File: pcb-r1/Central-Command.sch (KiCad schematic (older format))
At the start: 3 parts

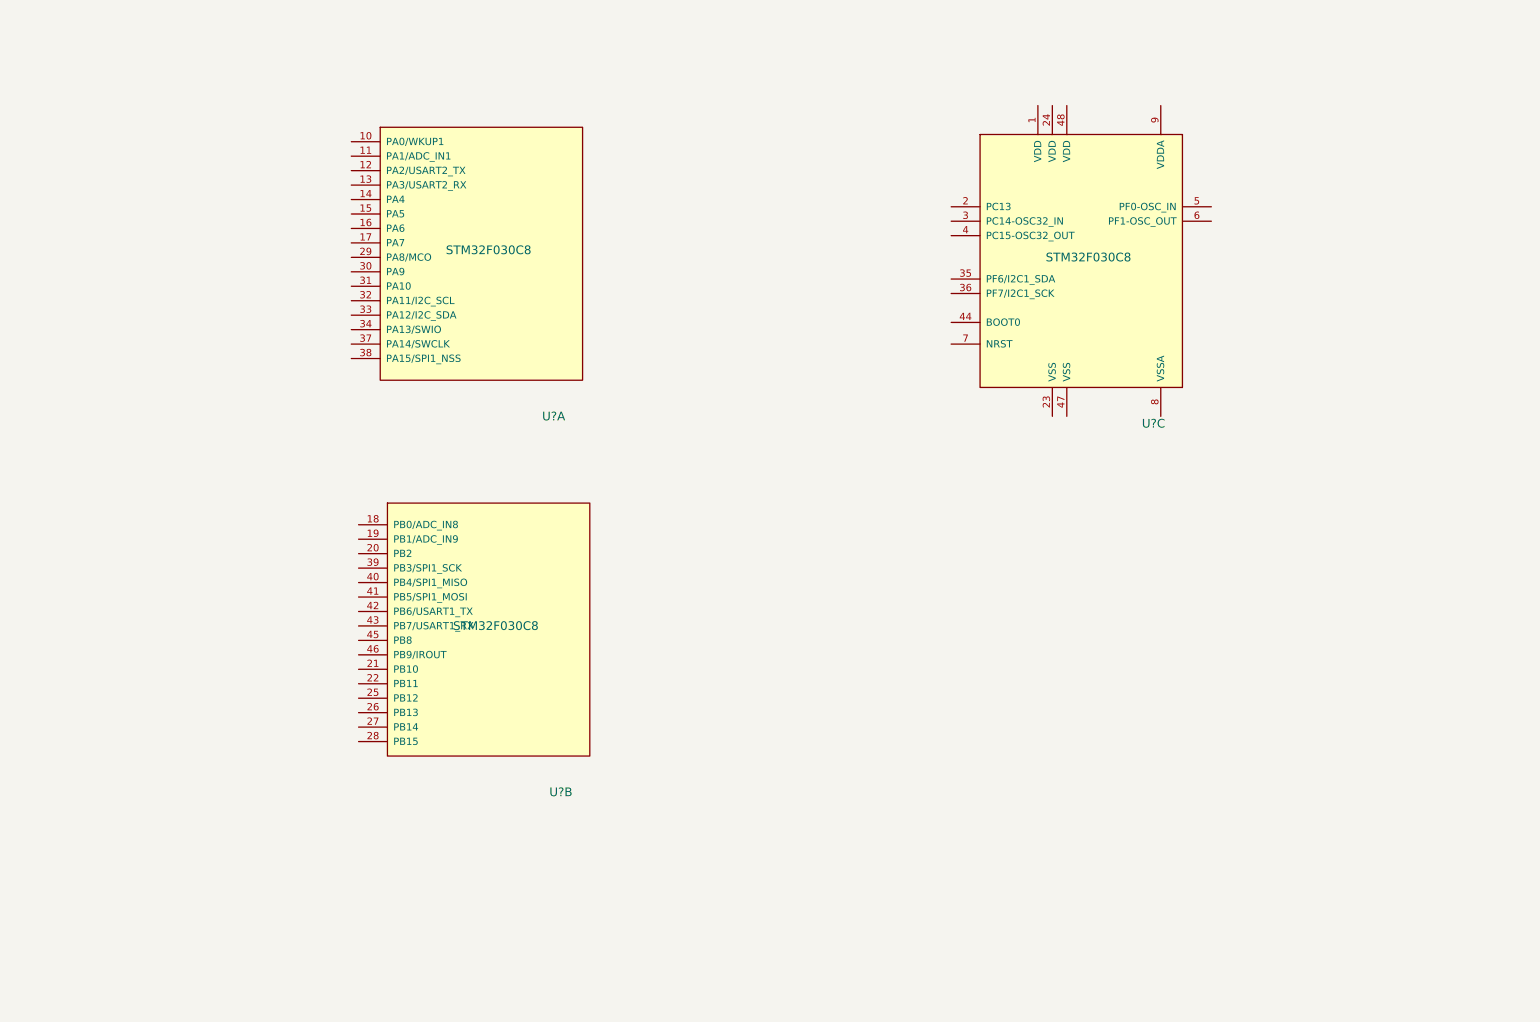
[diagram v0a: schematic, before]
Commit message: Updated the Micro symbol as per datasheet markup and started adding some more symols as per CC07-CC11
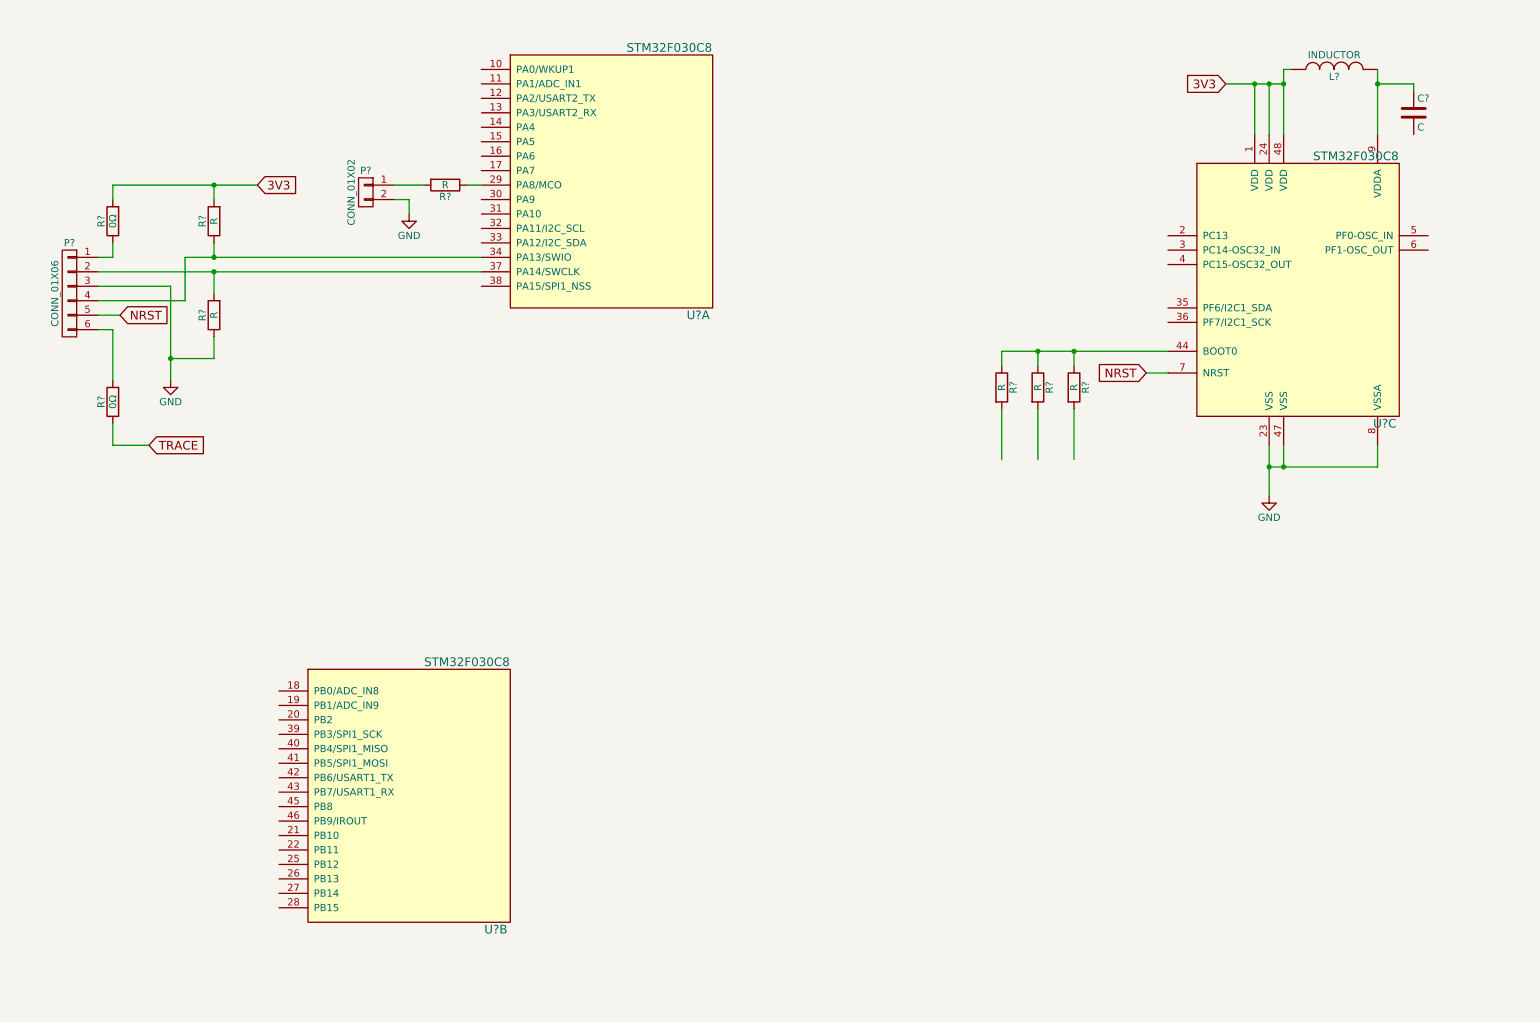
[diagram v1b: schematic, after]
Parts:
- removed U? (x3): STM32F030C8, symbol STM32F030C8
- added C?: C, symbol C
- added L?: INDUCTOR, symbol INDUCTOR
- added P?: CONN_01X02, symbol CONN_01X02
- added P?: CONN_01X06, symbol CONN_01X06
- added R? (x6): R, symbol R
- added R? (x2): 0Ω, symbol R
- added U? (x3): STM32F030C8, symbol STM32F030C8
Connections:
- net labels added: 3V3, GND, NRST, TRACE
- wire segments 0 -> 56

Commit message: Added linear voltage regulator
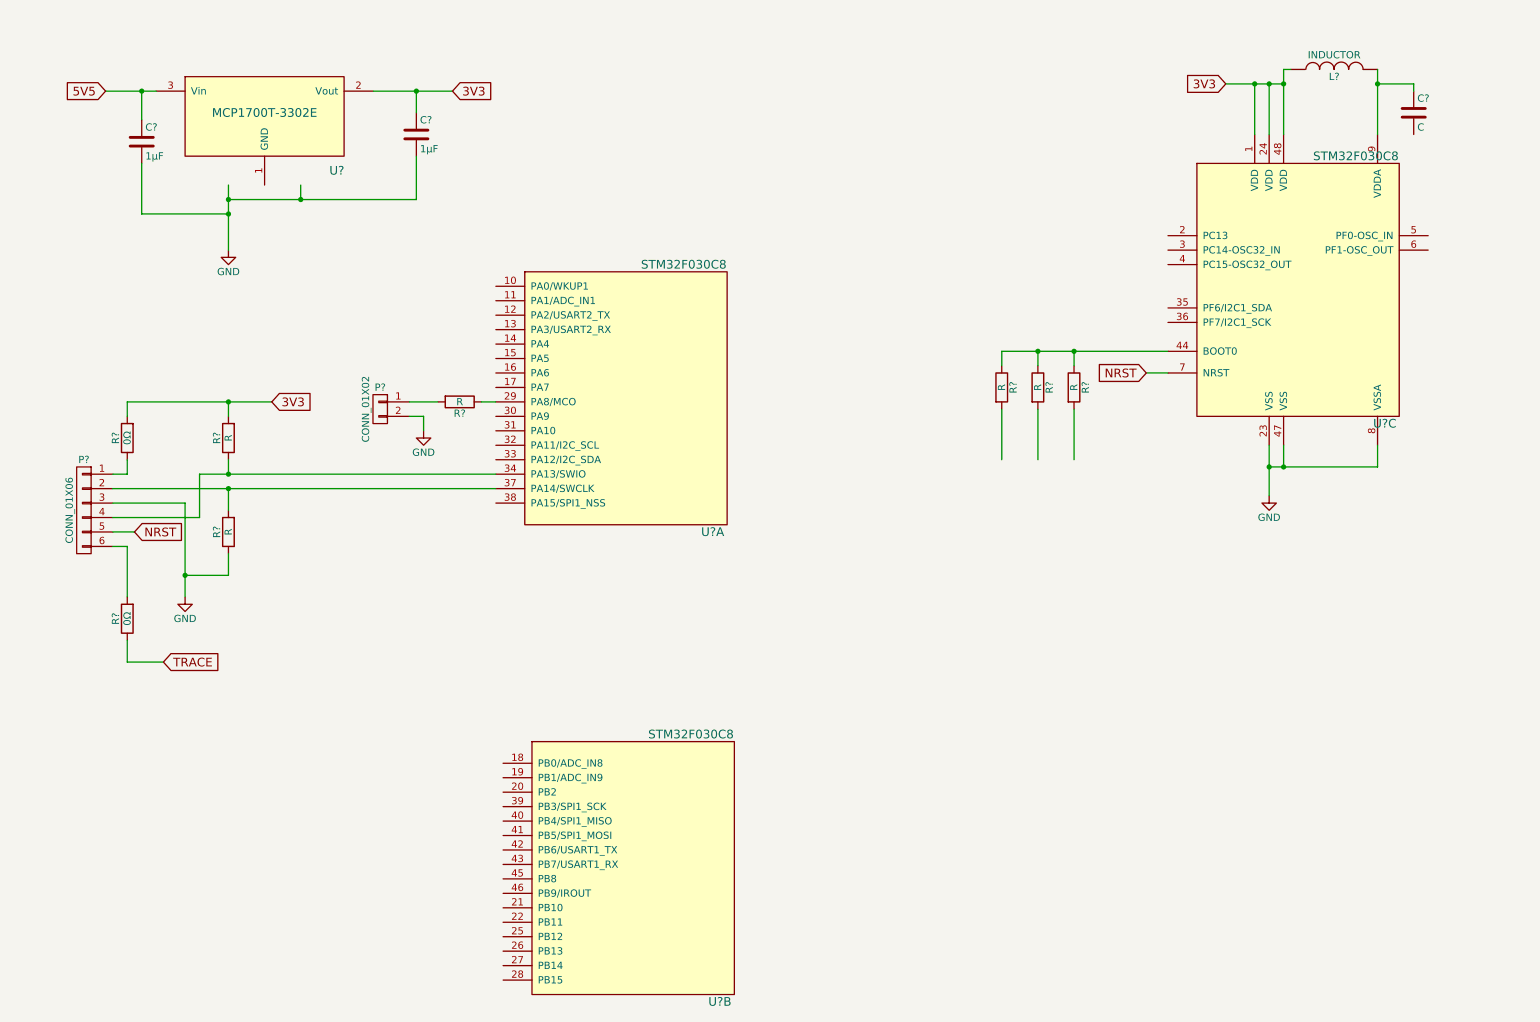
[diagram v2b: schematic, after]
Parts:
- added C? (x2): 1μF, symbol C
- added U?: MCP1700T-3302E, symbol MCP1700T-3302E
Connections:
- net labels added: 5V5
- wire segments 56 -> 71
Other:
- moved on the sheet: P?, R?, U?A, U?B

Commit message: Started layout to figure out sizes and features
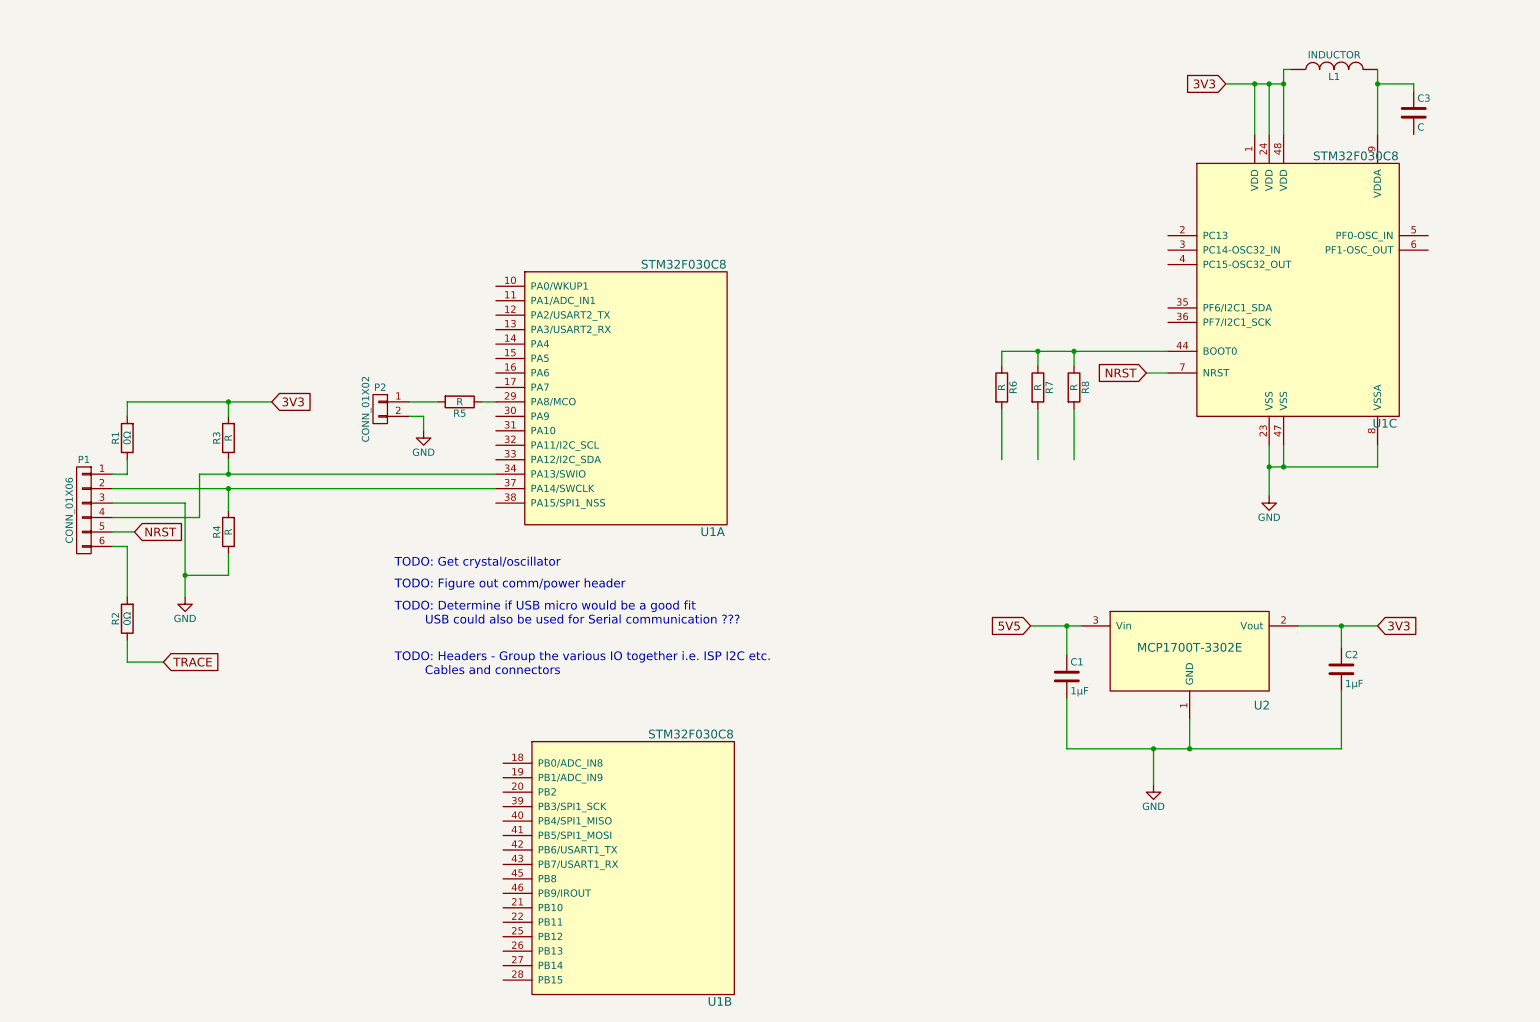
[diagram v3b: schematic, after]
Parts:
- C1, C2, C3: renamed from C?; footprint (none) -> Capacitors_SMD:C_0805
- L1: renamed from L?; footprint (none) -> Inductors_NEOSID:Neosid_Inductor_SM1206
- P1: renamed from P?; footprint (none) -> Pin_Headers:Pin_Header_Straight_1x06
- P2: renamed from P?; footprint (none) -> Pin_Headers:Pin_Header_Straight_1x02
- R1, R2, R3, R4, R5, R6, R7, R8: renamed from R?; footprint (none) -> Resistors_SMD:R_0805
- U1: renamed from U?; footprint (none) -> Housings_QFP:LQFP-48_7x7mm_Pitch0.5mm
- U2: renamed from U?; footprint (none) -> Housings_SOT-23_SOT-143_TSOT-6:SOT-23; link (none) -> http://parts.io/detail/1370896/MCP1700T-3302E%2FTT
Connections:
- wire segments 71 -> 53
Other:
- note added: "TODO: Determine if USB micro would be a good fit\n USB could also be used for Serial communication ???"
- note added: "TODO: Figure out comm/power header"
- note added: "TODO: Get crystal/oscillator"
- note added: "TODO: Headers - Group the various IO together i.e. ISP I2C etc.\n Cables and connectors"
- moved on the sheet: C1, C2, U2

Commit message: Updated for CC13 and CC14
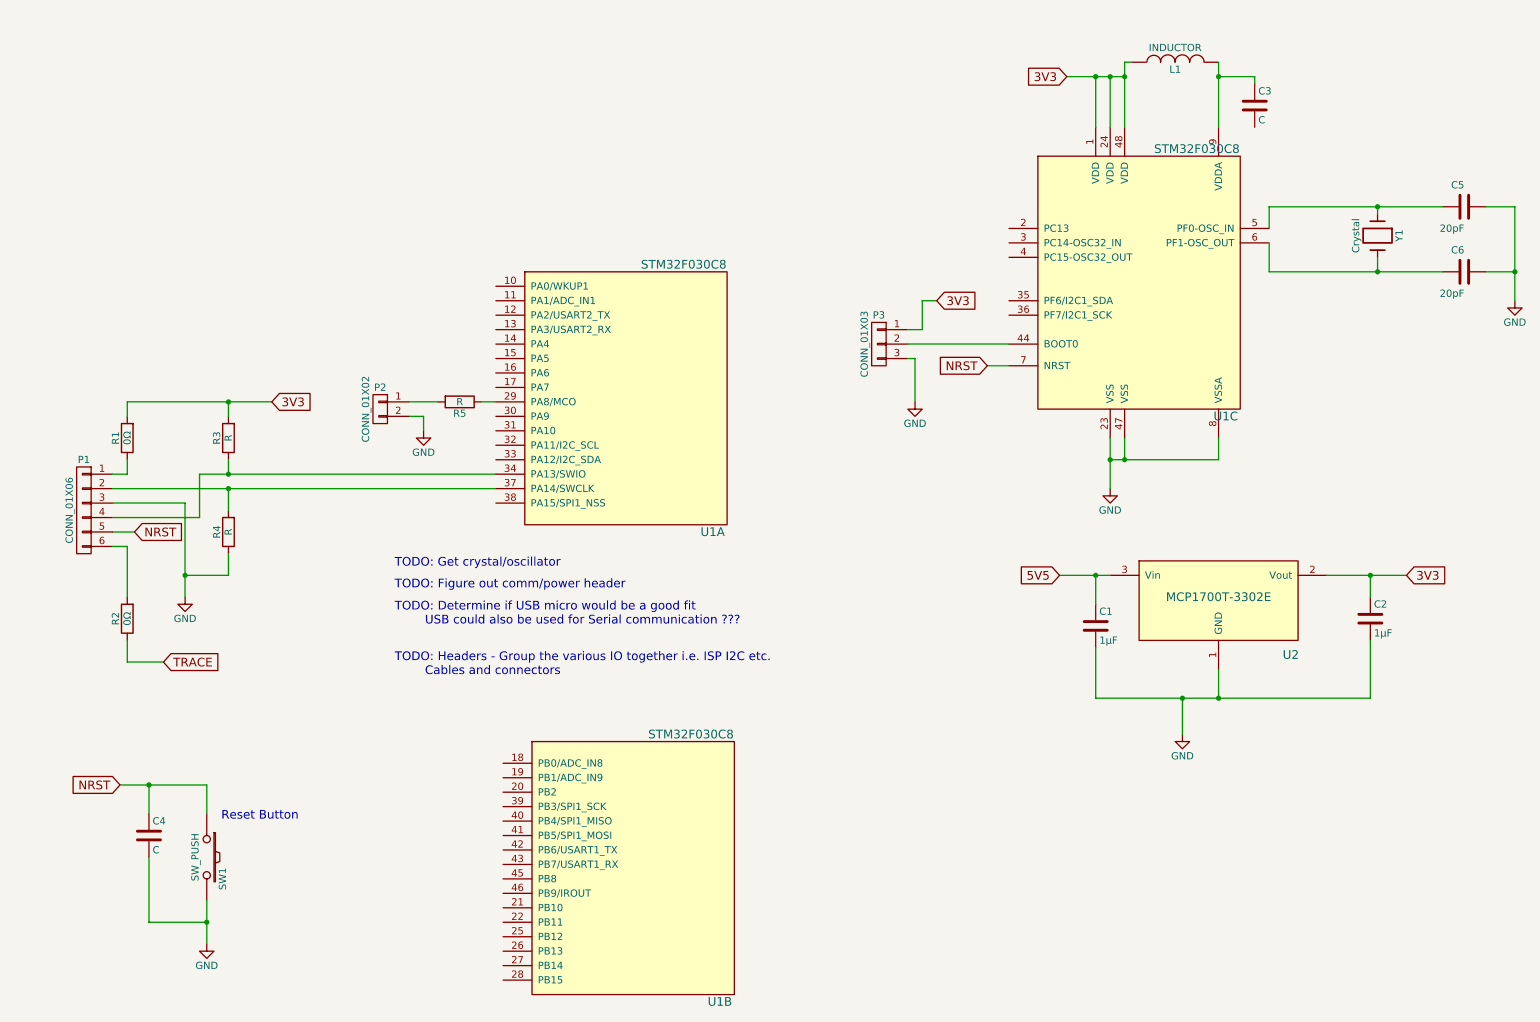
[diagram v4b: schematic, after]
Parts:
- removed R6, R7, R8: R, Resistors_SMD:R_0805, symbol R
- added C4: C, symbol C
- added C5, C6: 20pF, symbol C
- added P3: CONN_01X03, symbol CONN_01X03
- added SW1: SW_PUSH, symbol SW_PUSH
- added Y1: Crystal, symbol Crystal
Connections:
- wire segments 53 -> 67
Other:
- note added: "Reset Button"
- moved on the sheet: C1, C2, C3, L1, U1C, U2

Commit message: Added power block hierarchical sheet, FT232RQ and Micro-B USB symbols
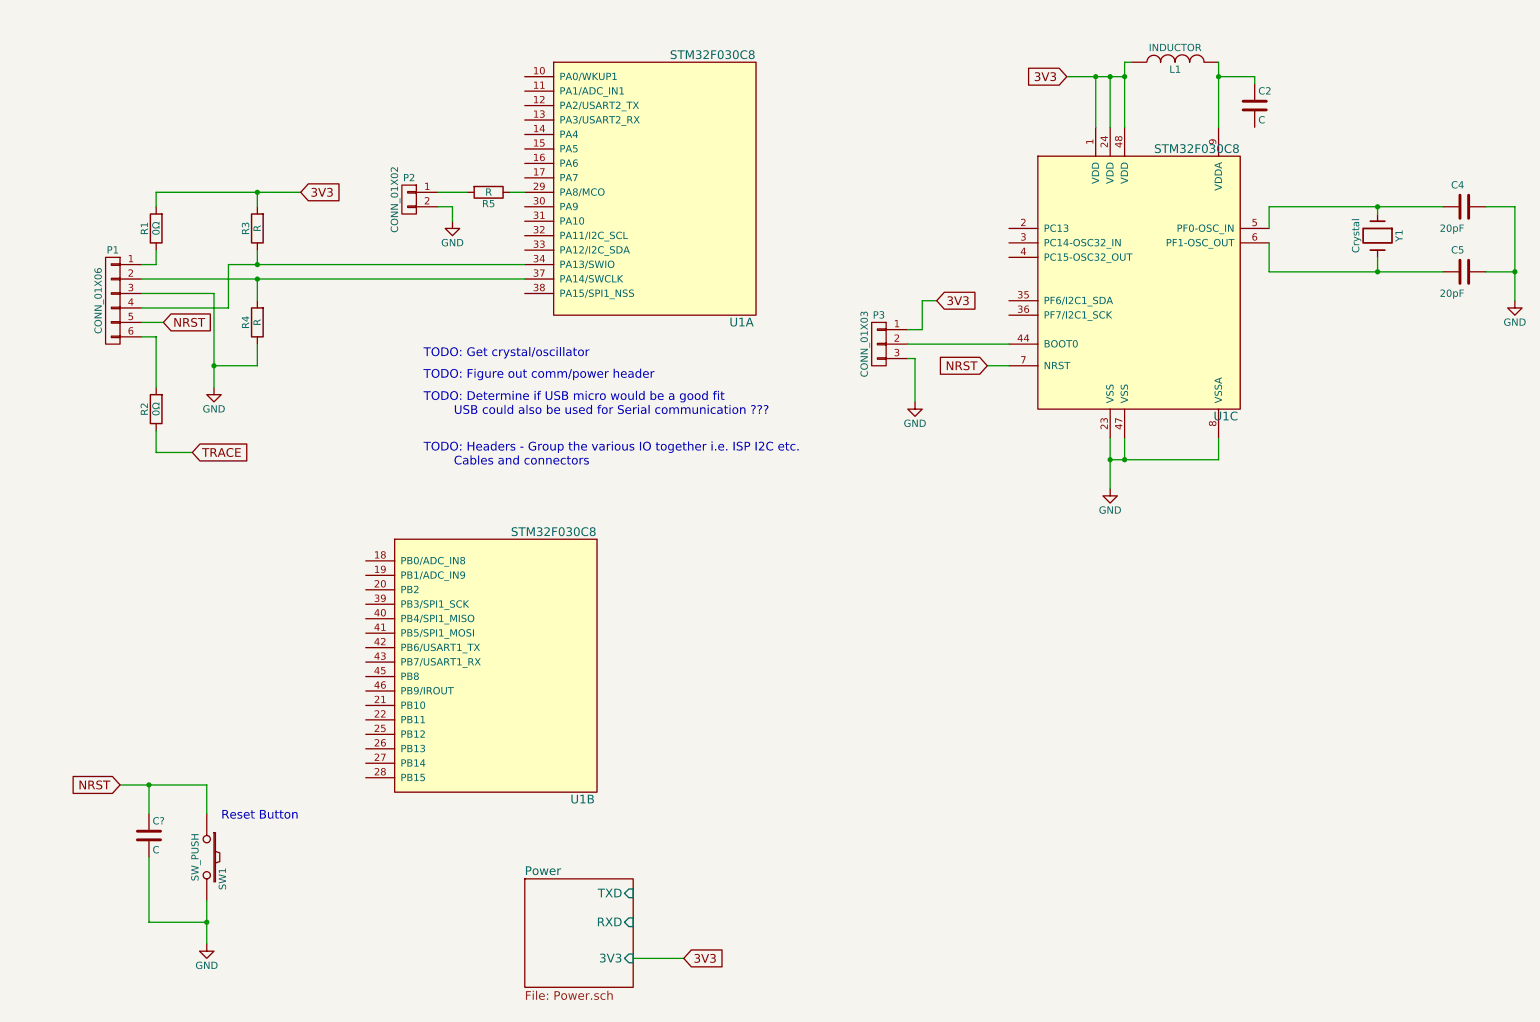
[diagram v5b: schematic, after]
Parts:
- removed C1, C2: 1μF, Capacitors_SMD:C_0805, symbol C
- removed U2: MCP1700T-3302E, Housings_SOT-23_SOT-143_TSOT-6:SOT-23, symbol MCP1700T-3302E
- renumbered C3 to C2, C5 to C4, C6 to C5, C4 to C?
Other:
- moved on the sheet: P1, P2, R1, R2, R3, R4, R5, U1A, U1B
